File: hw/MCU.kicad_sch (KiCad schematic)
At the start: 3 parts, among them IC3 STM32G071RBT6, J1 Conn_ARM_JTAG_SWD_10

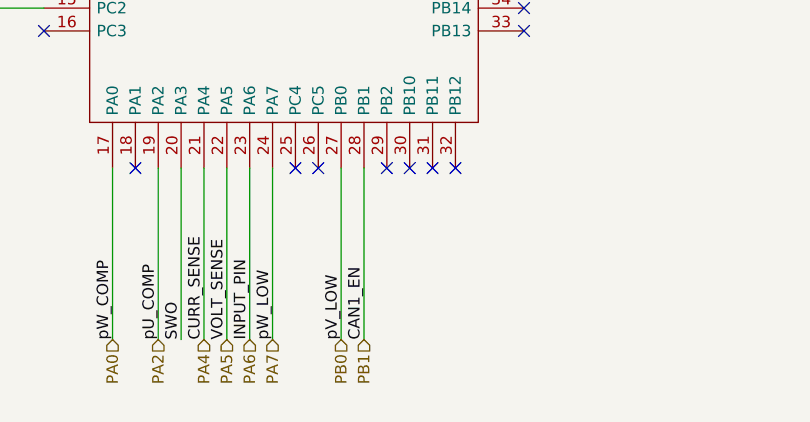
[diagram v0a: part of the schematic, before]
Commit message: connected interrupt pins to CAN controller
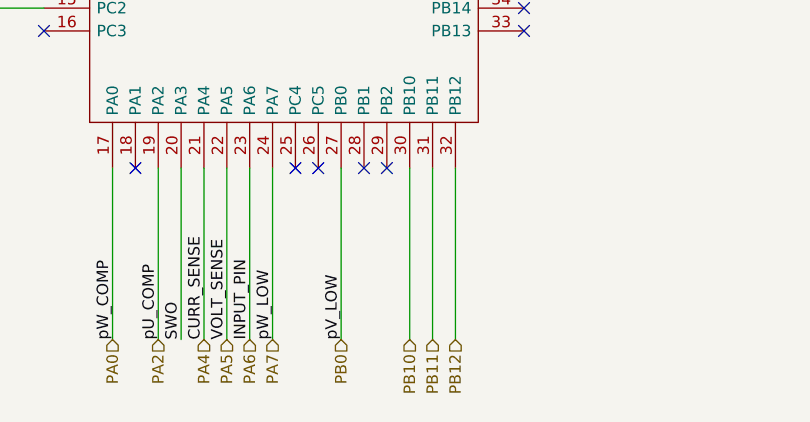
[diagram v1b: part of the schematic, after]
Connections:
- net PB10: now reaches IC3.30 (PB10)
- net PB11: now reaches IC3.31 (PB11)
- net PB12: now reaches IC3.32 (PB12)
- net PB1: no longer names the net of IC3.28 (PB1)
- no-connect marks 36 -> 34

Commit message: Revision V1.0
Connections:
- net PA10: now also IC3.42 (PA10); no longer IC3.44 (PA12_[PA10])
- net PA9: now also IC3.37 (PA9); no longer IC3.43 (PA11_[PA9])
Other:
- note removed: "Confirm pinouts!"
- note removed: "Why duplicated?"
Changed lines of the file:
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@@
   (no_connect (at 170.18 58.42))
   (no_connect (at 172.72 58.42))
+  (no_connect (at 182.88 86.36))
+  (no_connect (at 182.88 83.82))
   (no_connect (at 165.1 127))
   (no_connect (at 129.54 111.76))
@@
   (no_connect (at 182.88 96.52))
   (no_connect (at 182.88 99.06))
-  (no_connect (at 182.88 101.6))
   (no_connect (at 182.88 109.22))
   (no_connect (at 182.88 91.44))
-  (no_connect (at 182.88 88.9))
   (wire (pts (xy 182.88 76.2) (xy 209.55 76.2))
     (stroke (width 0) (type default) (color 0 0 0 0))
@@
     (stroke (width 0) (type default) (color 0 0 0 0))
   )
+  (wire (pts (xy 208.28 101.6) (xy 182.88 101.6))
+    (stroke (width 0) (type default) (color 0 0 0 0))
+  )
   (wire (pts (xy 170.18 127) (xy 170.18 146.05))
     (stroke (width 0) (type default) (color 0 0 0 0))
@@
     (stroke (width 0) (type default) (color 0 0 0 0))
   )
+  (wire (pts (xy 182.88 88.9) (xy 208.28 88.9))
+    (stroke (width 0) (type default) (color 0 0 0 0))
+  )
   (wire (pts (xy 182.88 104.14) (xy 208.28 104.14))
     (stroke (width 0) (type default) (color 0 0 0 0))
@@
     (stroke (width 0) (type default) (color 0 0 0 0))
   )
-  (wire (pts (xy 182.88 83.82) (xy 208.28 83.82))
-    (stroke (width 0) (type default) (color 0 0 0 0))
-  )
   (wire (pts (xy 119.38 101.6) (xy 129.54 101.6))
     (stroke (width 0) (type default) (color 0 0 0 0))
@@
   )
   (wire (pts (xy 228.6 22.86) (xy 228.6 24.13))
-    (stroke (width 0) (type default) (color 0 0 0 0))
-  )
-  (wire (pts (xy 208.28 86.36) (xy 182.88 86.36))
     (stroke (width 0) (type default) (color 0 0 0 0))
   )
@@
     (effects (font (size 1.27 1.27)) (justify left bottom))
   )
-  (text "Why duplicated?\n" (at 76.2 101.6 0)
-    (effects (font (size 1.27 1.27)) (justify left bottom))
-  )
-  (text "Confirm pinouts!\n" (at 134.62 34.29 0)
-    (effects (font (size 1.27 1.27)) (justify left bottom))
-  )
   (text "#ifdef     HARDWARE_GROUP_G0_H\n\n#define    MCU_G071\n#define    N_VARIANT\n#define    USE_TIMER_16_CHANNEL_1\n#define    INPUT_PIN               LL_GPIO_PIN_6\n#define    INPUT_PIN_PORT              GPIOA\n#define    IC_TIMER_CHANNEL         LL_TIM_CHANNEL_CH1\n#define    IC_TIMER_REGISTER          TIM16\n#define    IC_TIMER_POINTER           htim16\n\n#define    INPUT_DMA_CHANNEL       LL_DMA_CHANNEL_1\n#define    DMA_HANDLE_TYPE_DEF     hdma_tim16_ch1\n#define    IC_DMA_IRQ_NAME         DMA1_Channel1_IRQn\n\n#define PHASE_B_GPIO_LOW          LL_GPIO_PIN_0\n#define PHASE_B_GPIO_PORT_LOW         GPIOB\n#define PHASE_B_GPIO_HIGH          LL_GPIO_PIN_9\n#define PHASE_B_GPIO_PORT_HIGH         GPIOA\n\n#define PHASE_A_GPIO_LOW          LL_GPIO_PIN_15\n#define PHASE_A_GPIO_PORT_LOW         GPIOB\n#define PHASE_A_GPIO_HIGH          LL_GPIO_PIN_10\n#define PHASE_A_GPIO_PORT_HIGH         GPIOA\n\n#define PHASE_C_GPIO_LOW          LL_GPIO_PIN_7\n#define PHASE_C_GPIO_PORT_LOW         GPIOA\n#define PHASE_C_GPIO_HIGH          LL_GPIO_PIN_8\n#define PHASE_C_GPIO_PORT_HIGH         GPIOA\n\n#define PHASE_B_COMP  LL_COMP_INPUT_MINUS_IO2  // pb7\n#define PHASE_A_COMP  LL_COMP_INPUT_MINUS_IO3  // pa2\n#define PHASE_C_COMP  LL_COMP_INPUT_MINUS_IO3  // pa0\n\n#define PHASE_A_EXTI_LINE           LL_EXTI_LINE_18\n#define PHASE_A_COMP_NUMBER         COMP2\n\n#define PHASE_B_EXTI_LINE           LL_EXTI_LINE_18\n#define PHASE_B_COMP_NUMBER         COMP2\n\n#define PHASE_C_EXTI_LINE           LL_EXTI_LINE_17\n#define PHASE_C_COMP_NUMBER         COMP1\n\n#define VOLTAGE_ADC_PIN     LL_GPIO_PIN_5\n#define VOLTAGE_ADC_CHANNEL LL_ADC_CHANNEL_5\n\n#define CURRENT_ADC_PIN     LL_GPIO_PIN_4\n#define CURRENT_ADC_CHANNEL  LL_ADC_CHANNEL_4"
     (at 17.78 123.19 0)
@@
     (effects (font (size 1.27 1.27)) (justify left bottom))
   )
+  (label "pV_HIGH" (at 208.28 101.6 180)
+    (effects (font (size 1.27 1.27)) (justify right bottom))
+  )
   (label "NRST" (at 246.38 31.75 180)
     (effects (font (size 1.27 1.27)) (justify right bottom))
@@
     (effects (font (size 1.27 1.27)) (justify left bottom))
   )
-  (label "pU_HIGH" (at 208.28 83.82 180)
-    (effects (font (size 1.27 1.27)) (justify right bottom))
-  )
   (label "pV_LOW" (at 162.56 146.05 90)
     (effects (font (size 1.27 1.27)) (justify left bottom))
@@
     (effects (font (size 1.27 1.27)) (justify right bottom))
   )
-  (label "pV_HIGH" (at 208.28 86.36 180)
-    (effects (font (size 1.27 1.27)) (justify right bottom))
-  )
   (label "NRST" (at 119.38 101.6 0)
     (effects (font (size 1.27 1.27)) (justify left bottom))
@@
     (effects (font (size 1.27 1.27)) (justify right bottom))
   )
+  (label "pU_HIGH" (at 208.28 88.9 180)
+    (effects (font (size 1.27 1.27)) (justify right bottom))
+  )
   (hierarchical_label "PB3" (shape input) (at 154.94 44.45 90)
     (effects (font (size 1.27 1.27)) (justify left))
@@
     (effects (font (size 1.27 1.27)) (justify right))
   )
+  (hierarchical_label "PA9" (shape input) (at 208.28 101.6 0)
+    (effects (font (size 1.27 1.27)) (justify left))
+  )
   (hierarchical_label "PB12" (shape input) (at 175.26 146.05 270)
     (effects (font (size 1.27 1.27)) (justify right))
@@
     (effects (font (size 1.27 1.27)) (justify left))
   )
-  (hierarchical_label "PA10" (shape input) (at 208.28 83.82 0)
-    (effects (font (size 1.27 1.27)) (justify left))
-  )
   (hierarchical_label "PC1" (shape input) (at 119.38 106.68 180)
     (effects (font (size 1.27 1.27)) (justify right))
@@
     (effects (font (size 1.27 1.27)) (justify right))
   )
+  (hierarchical_label "PA10" (shape input) (at 208.28 88.9 0)
+    (effects (font (size 1.27 1.27)) (justify left))
+  )
   (hierarchical_label "PD6" (shape input) (at 157.48 44.45 90)
     (effects (font (size 1.27 1.27)) (justify left))
@@
     (effects (font (size 1.27 1.27)) (justify left))
   )
-  (hierarchical_label "PA9" (shape input) (at 208.28 86.36 0)
-    (effects (font (size 1.27 1.27)) (justify left))
-  )

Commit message: commenting
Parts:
- removed IC3: STM32G071RBT6, QFP50P1200X1200X160-64N, symbol MAG_MCUs:STM32G071RBT6
- added R25: R, symbol Device:R
- added U11: STM32G071GBU6, UFQFPN-28, symbol MAG_MCUs:STM32G071GBU6
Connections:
- net +3V3: now also R25.1, U11.3 (VDD)
- net GND: now also U11.4 (VSS)
- net NRST: now also R25.2, U11.5 (PF2-NRST)
- net PA10: now also U11.19 (PA12[PA10])
- net PA2: now also U11.8 (PA2)
- net PA5: now also U11.11 (PA5)
- net PA7: now also U11.13 (PA7)
- net PA8: now also U11.16 (PA8)
- net PA9: now also U11.18 (PA11[PA9])
- net PB0: now also U11.14 (PB0)
- net PB3: now also U11.23 (PB3)
- net PB4: now also U11.24 (PB4)
- net PB7: now also U11.27 (PB7)
- net SWCLK: now also U11.21 (PA14-BOOT0)
- net SWDIO: now also U11.20 (PA13)
- net SWO: now also U11.9 (PA3)
- net TDI: now also U11.22 (PA15)
- new net PA1: U11.7 (PA1)
- new net PB1: U11.15 (PB1)
- no-connect marks 34 -> 9
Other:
- note added: "#ifdef HARDWARE_GROUP_G0_I #define MCU_G071 #define USE_TIMER_3_CHANNEL_1 #define INPUT_PIN LL_GPIO_PIN_4 #define INPUT_PIN_PORT GPIOB #define IC_TIMER_CHANNEL LL_TIM_CHANNEL_CH1 #define IC_TIMER_REGISTER TIM3 #define IC_TIMER_POINTER htim3 #define INPUT_DMA_CHANNEL LL_DMA_CHANNEL_1 #define DMA_HANDLE_TYPE_DEF hdma_tim3_ch1 #define IC_DMA_IRQ_NAME DMA1_Channel1_IRQn #define PHASE_A_GPIO_LOW LL_GP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"
- note added: "CURRENT_ADC"
- note added: "FIX FOOTPRINT?"
- note added: "PHA_COMP"
- note added: "PHA_HIGH"
- note added: "PHA_LOW"
- note added: "PHB_COMP"
- note added: "PHB_HIGH"
- note added: "PHB_LOW"
- note added: "PHC_COMP"
- note added: "PHC_HIGH"
- note added: "PHC_LOW"
- note added: "SERVO_INPUT"
- note added: "VOLTAGE_ADC"
- note removed: "#ifdef HARDWARE_GROUP_G0_H #define MCU_G071 #define N_VARIANT #define USE_TIMER_16_CHANNEL_1 #define INPUT_PIN LL_GPIO_PIN_6 #define INPUT_PIN_PORT GPIOA #define IC_TIMER_CHANNEL LL_TIM_CHANNEL_CH1 #define IC_TIMER_REGISTER TIM16 #define IC_TIMER_POINTER htim16 #define INPUT_DMA_CHANNEL LL_DMA_CHANNEL_1 #define DMA_HANDLE_TYPE_DEF hdma_tim16_ch1 #define IC_DMA_IRQ_NAME DMA1_Channel1_IRQn #define 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"
- moved on the sheet: C5, J1
